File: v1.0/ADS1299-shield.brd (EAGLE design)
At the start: 63.5 x 25.4 mm, 32 parts, among them IC1 ADS1298*PAG*, IC2 TPS73250DBVT, IC3 TPS73233DBVT

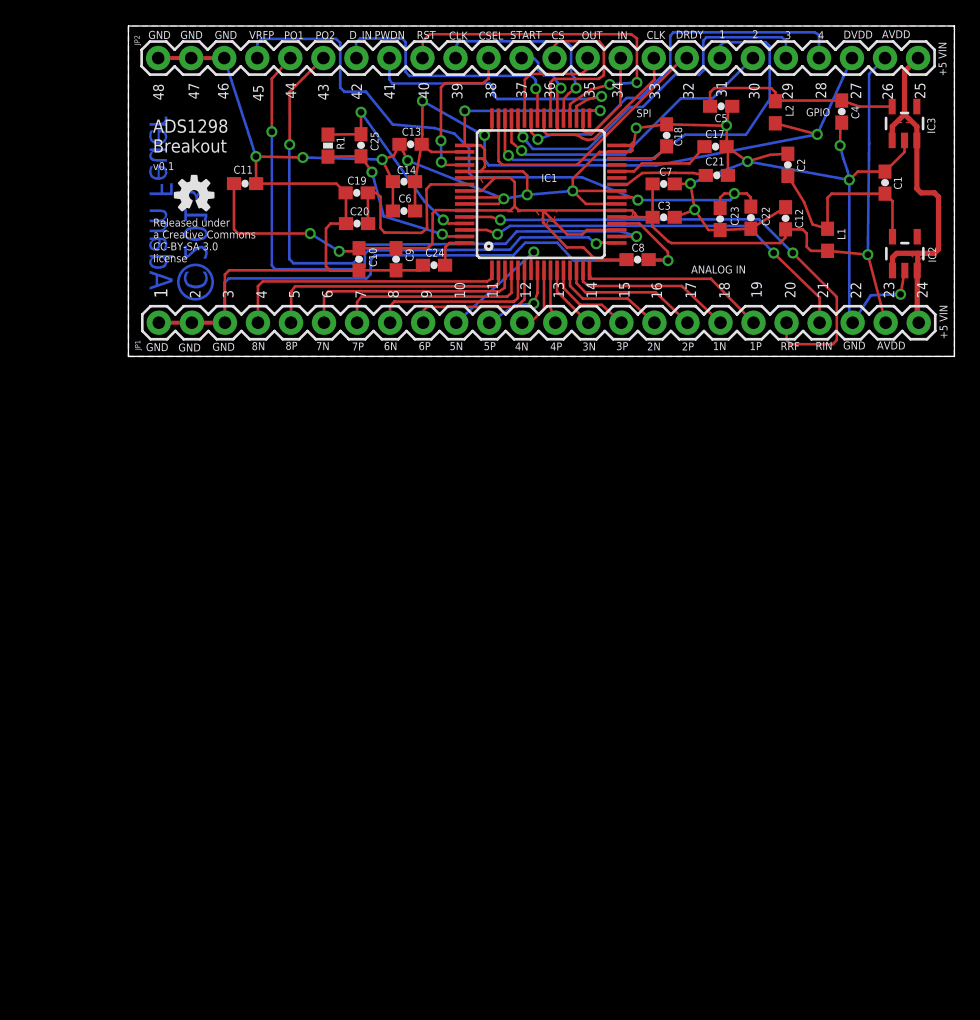
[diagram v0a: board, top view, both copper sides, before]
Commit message: schematic work - power supplies and decoupling done; updated ADS1299 library symbol to better organize pinouts; minor updates to power supply libraries
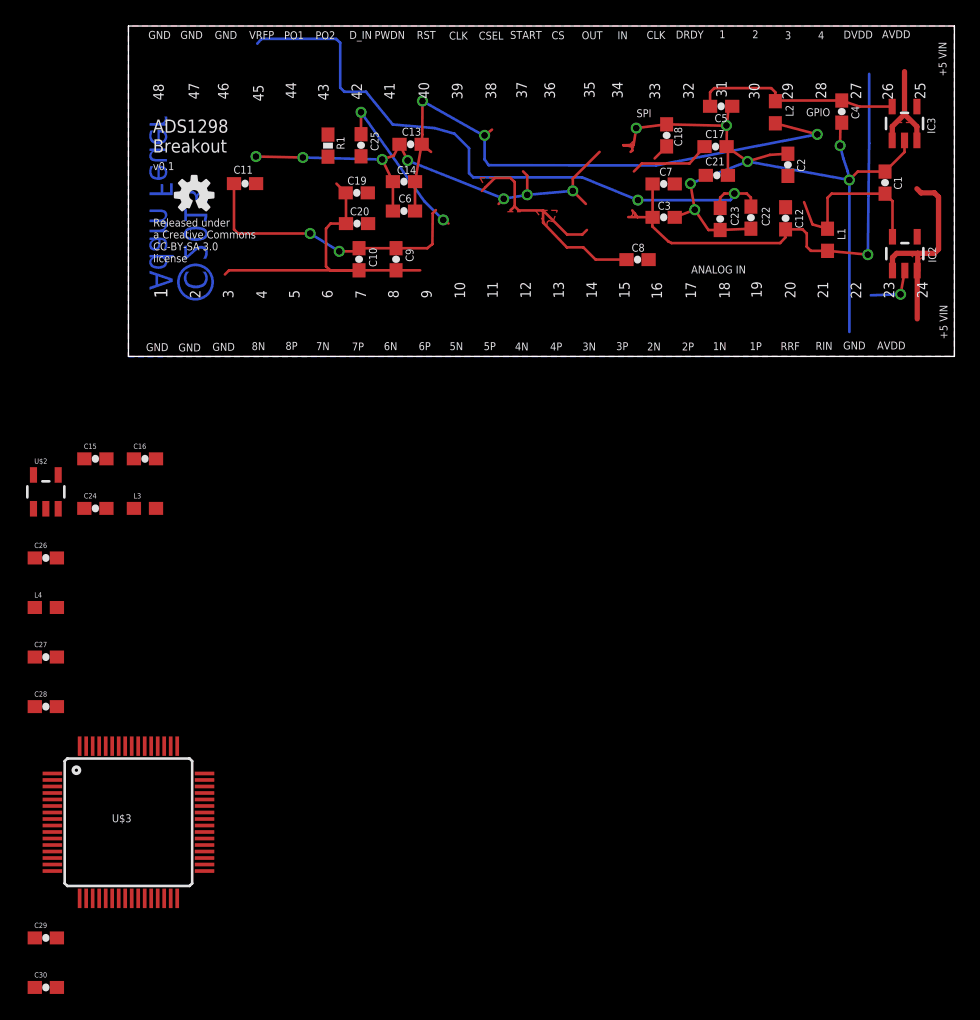
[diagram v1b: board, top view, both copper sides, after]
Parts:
- removed IC1: ADS1298*PAG*, burr-brown-5a:TQFP64
- removed JP1, JP2: M24, SparkFun-Connectors:1X24
- added C15: 2.2uF, SparkFun-Passives:0603-CAP
- added C16: 10 uF, SparkFun-Passives:0603-CAP
- added C26, C28, C29, C30: 1uF, SparkFun-Passives:0603-CAP
- added C27: 10uf, SparkFun-Passives:0603-CAP
- added L3, L4: 3.3 uH, SparkFun-Passives:0603
- added U$2: TPS604XXDBV, TPS604xx:SOT23-5
- added U$3: ADS1299*PAG*, ADS129x:TQFP64
- C17: value 22uF -> 100uF
- C24: value 100pF -> 10uf
- IC2: value TPS73250DBVT -> TPS73225DBVT
- moved C24 32.1 mm to (-2.54, -11.4), turned to 0 degrees
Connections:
- removed net PACEOUT1: IC1.17, JP2.6
- removed net PACEOUT2: IC1.18, JP2.7
- removed net RLD_IN: IC1.62, JP1.22
- removed net RLD_INV: C25.2, IC1.61, R1.2
- removed net RLD_OUT: C25.1, IC1.63, R1.1
- removed net RLD_REF: IC1.60, JP1.21
- removed net VCC: IC2.1, IC2.3, IC3.1, IC3.3, JP1.25, JP2.25
- new net AVSS: C11.2, C12.2, C29.2, C30.2, U$3.20, U$3.23, U$3.32, U$3.53, U$3.57, U$3.58
- new net BIASIN: U$3.62
- new net BIASINV: C25.2, R1.2, U$3.61
- new net BIASOUT: C25.1, R1.1, U$3.63
- new net BIASREF: U$3.60
- new net GND: C27.1, C28.1, C7.2, C8.2, IC2.1, IC2.3, IC3.1, IC3.3, L4.1
- new net N$10: C26.1, U$2.3
- new net N$12: L4.2, U$2.2
- new net N$9: C26.2, U$2.5
- new net SRB1: U$3.18
- new net SRB2: U$3.17
- new net VCC_-5V: C24.1, L3.2
- net !PWDN: now also U$3.35; no longer IC1.35, JP2.9
- net !RESET: now also U$3.36; no longer IC1.36, JP2.10
- net AGND: now also C15.2, C16.2, C27.2, C28.2, C29.1, C30.1, U$2.4, U$3.25, U$3.33, U$3.49, U$3.51; no longer C11.2, C12.2, C7.2, C8.2, IC1.20, IC1.23, IC1.25, IC1.31, IC1.32, IC1.33, IC1.49, IC1.51, IC1.53, IC1.57, IC1.58, JP1.2, JP1.23, JP1.3, JP1.4, JP2.2, JP2.3, JP2.4
- net AVDD: now also U$3.19, U$3.21, U$3.22, U$3.54, U$3.56, U$3.59; no longer IC1.19, IC1.21, IC1.22, IC1.54, IC1.56, IC1.59, JP1.24, JP2.24
- net CLK: now also U$3.37; no longer IC1.37, JP2.11
- net CLKSEL: now also U$3.52; no longer IC1.52, JP2.12
- net DAISY_IN: now also U$3.41; no longer IC1.41, JP2.8
- net DVDD: now also U$3.48, U$3.50; no longer IC1.48, IC1.50, JP2.23
- net GPIO1: now also U$3.42; no longer IC1.42, JP2.22
- net GPIO2: now also U$3.44; no longer IC1.44, JP2.21
- net GPIO3: now also U$3.45; no longer IC1.45, JP2.20
- net GPIO4: now also U$3.46; no longer IC1.46, JP2.19
- net IN1N: now also U$3.15; no longer IC1.15, JP1.19
- net IN1P: now also U$3.16; no longer IC1.16, JP1.20
- net IN2N: now also U$3.13; no longer IC1.13, JP1.17
- net IN2P: now also U$3.14; no longer IC1.14, JP1.18
- net IN3N: now also U$3.11; no longer IC1.11, JP1.15
- net IN3P: now also U$3.12; no longer IC1.12, JP1.16
- net IN4N: now also U$3.9; no longer IC1.9, JP1.13
- net IN4P: now also U$3.10; no longer IC1.10, JP1.14
- net IN5N: now also U$3.7; no longer IC1.7, JP1.11
- net IN5P: now also U$3.8; no longer IC1.8, JP1.12
- net IN6N: now also U$3.5; no longer IC1.5, JP1.9
- net IN6P: now also U$3.6; no longer IC1.6, JP1.10
- net IN7N: now also U$3.3; no longer IC1.3, JP1.7
- net IN7P: now also U$3.4; no longer IC1.4, JP1.8
- net IN8N: now also U$3.1; no longer IC1.1, JP1.5
- net IN8P: now also U$3.2; no longer IC1.2, JP1.6
- net N$3: now also U$3.28; no longer IC1.28
- net N$4: now also U$3.30; no longer IC1.30
- net N$5: now also U$3.55; no longer IC1.55
- net N$7: now also C15.1, C16.1, L3.1, U$2.1; no longer C24.1, IC1.64
- net N$8: now also U$3.26; no longer IC1.26
- net SPI_CLK: now also U$3.40; no longer IC1.40, JP2.17
- net SPI_CS: now also U$3.39; no longer IC1.39, JP2.14
- net SPI_DRDY: now also U$3.47; no longer IC1.47, JP2.18
- net SPI_IN: now also U$3.34; no longer IC1.34, JP2.16
- net SPI_OUT: now also U$3.43; no longer IC1.43, JP2.15
- net SPI_START: now also U$3.38; no longer IC1.38, JP2.13
- net VREFP: now also U$3.24; no longer IC1.24, JP2.5
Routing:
- net AGND: track 257.5 -> 133.2 mm, vias 18 -> 15
- net PACEOUT2: track 46.4 -> 0.00 mm, vias 2 -> 0
- net PACEOUT1: track 44.9 -> 0.00 mm, vias 2 -> 0
- net RLD_REF: track 39.9 -> 0.00 mm, vias 2 -> 0
- net GPIO4: track 34.4 -> 0.00 mm, vias 1 -> 0
- net RLD_IN: track 31.8 -> 0.00 mm, vias 2 -> 0
- net GPIO1: track 30.1 -> 0.00 mm, vias 1 -> 0
- net VCC: track 29.4 -> 0.00 mm
- net GPIO2: track 28.5 -> 0.00 mm, vias 1 -> 0
- net !RESET: track 28.1 -> 0.00 mm, vias 2 -> 0
- net AVDD: track 108.2 -> 81.7 mm
- net GND: track 0.00 -> 23.9 mm
- net GPIO3: track 23.8 -> 0.00 mm, vias 1 -> 0
- net !PWDN: track 22.0 -> 0.00 mm, vias 1 -> 0
- net IN8N: track 21.6 -> 0.00 mm
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
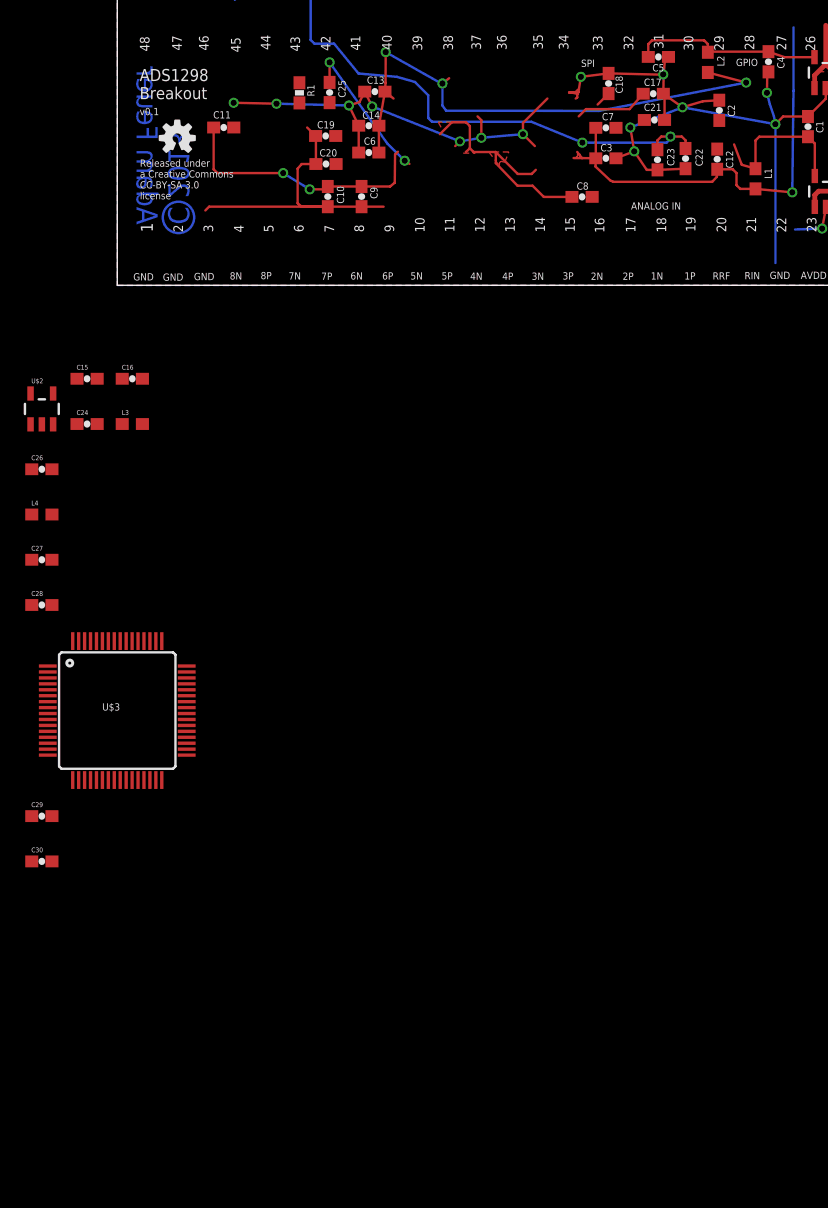
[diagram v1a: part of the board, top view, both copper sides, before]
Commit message: updated ads1299 library to have NAME and VALUE; improved power supply section, including supply-select jumpers
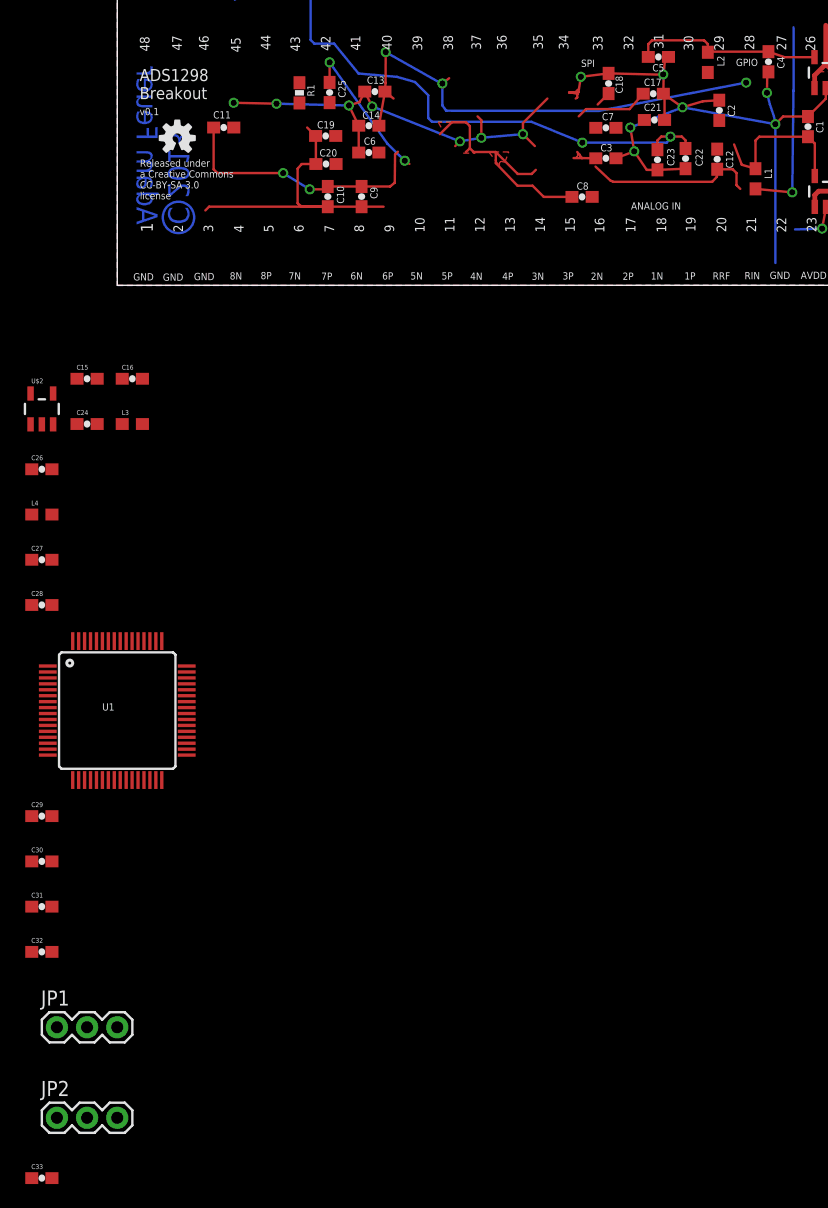
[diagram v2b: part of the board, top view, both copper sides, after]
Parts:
- added C31, C32: 1uF, SparkFun-Passives:0603-CAP
- added C33: 0.1uF, SparkFun-Passives:0603-CAP
- added JP1: AVDD_5V-2.5V, SparkFun-Passives:1X03
- added JP2: AVSS_-2.5V-GND, SparkFun-Passives:1X03
- IC2: value TPS73225DBVT -> TPS72325DBVT
- IC3: value TPS73233DBVT -> TPS73225DBVT
- U1: value ADS1299*PAG* -> ADS1299IPAG
- renumbered U$3 to U1
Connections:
- new net +2.5V: C6.1, JP1.3, L2.2
- new net -2.5V: C3.1, JP2.1, L1.2
- new net N$11: C32.1, IC3.4
- new net N$13: C31.1, IC2.4
- new net VCC_5V: C27.1, IC3.1, IC3.3, JP1.1, L4.1
- net AGND: now also C31.2, C32.2, JP2.3
- net AVDD: now also C33.1, JP1.2; no longer C3.1, L1.2
- net AVSS: now also C33.2, JP2.2
- net DVDD: no longer C6.1, L2.2
- net GND: no longer C27.1, C28.1, IC2.1, IC2.3, IC3.1, IC3.3, L4.1
- net VCC_-5V: now also C28.1, IC2.1, IC2.3
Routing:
- net AVDD: track 81.7 -> 57.6 mm, vias 3 -> 2
- net GND: track 23.9 -> 0.00 mm
- net -2.5V: track 0.00 -> 19.5 mm, vias 0 -> 1
- net VCC_-5V: track 0.00 -> 15.8 mm
- net VCC_5V: track 0.00 -> 8.09 mm
- net DVDD: track 46.9 -> 41.3 mm

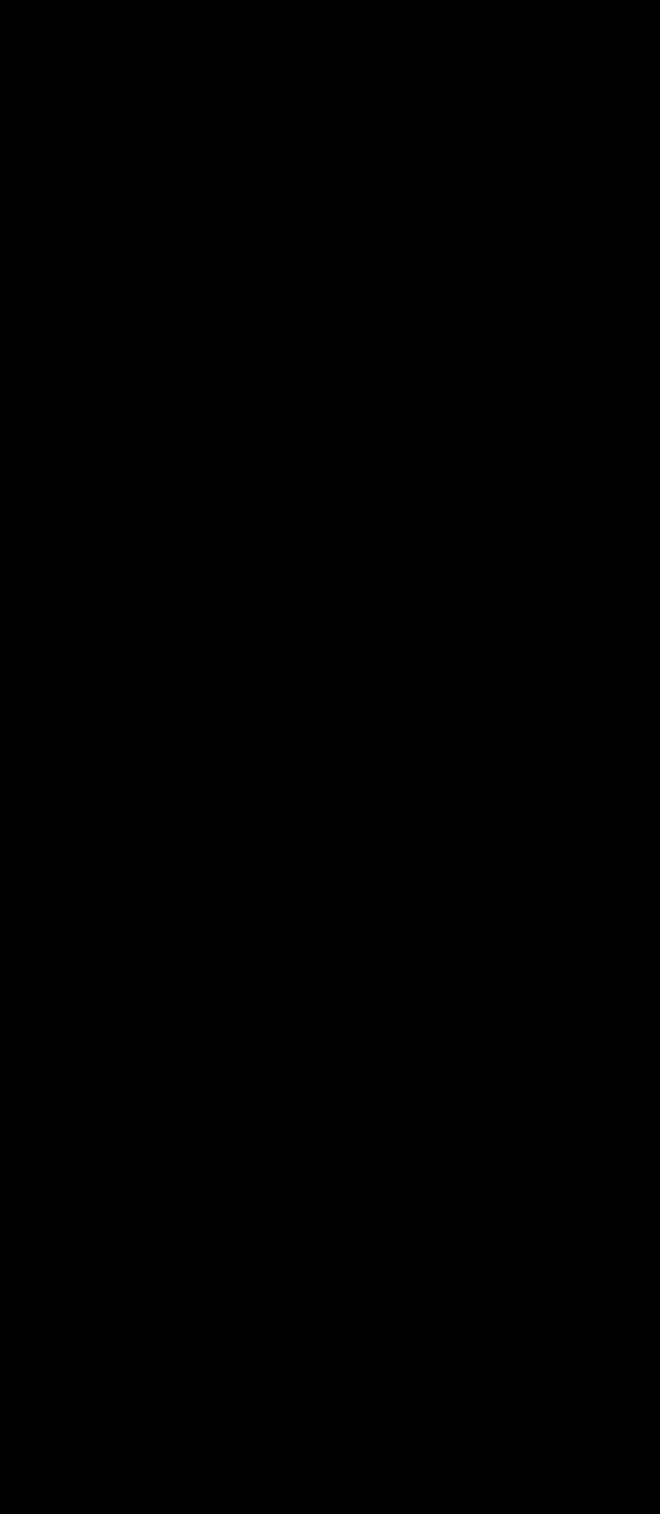
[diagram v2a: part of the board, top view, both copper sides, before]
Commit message: input filtering section done
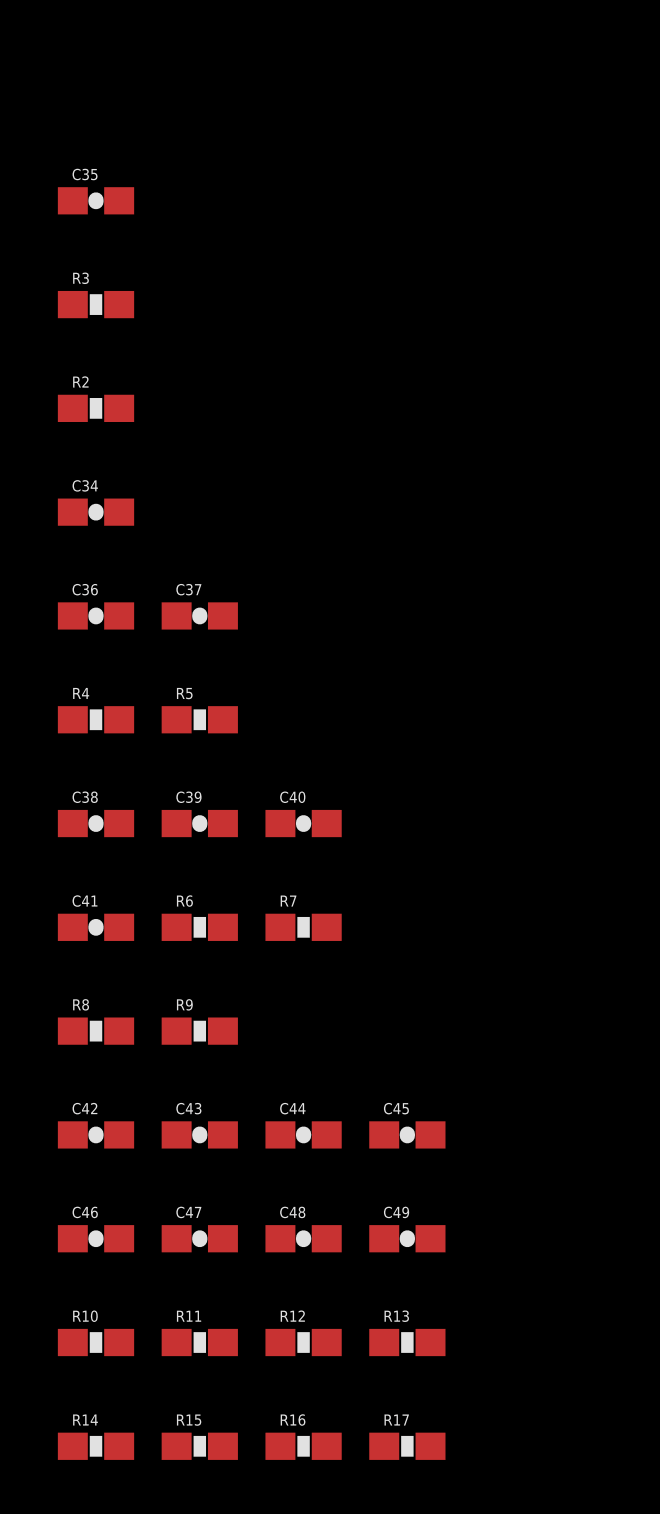
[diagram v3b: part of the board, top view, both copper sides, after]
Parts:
- added C34, C35, C36, C37, C38, C39, C40, C41, C42, C43, C44, C45, C46, C47, C48, C49: 4.7nF, SparkFun-Passives:0603-CAP
- added R10, R11, R12, R13, R14, R15, R16, R17, R2, R3, R4, R5, R6, R7, R8, R9: 4.99k, SparkFun-Passives:0603-RES
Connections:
- new net AIN1N: C34.2, C37.2, C43.2, R11.2, R2.2, R5.2
- new net AIN1P: C35.1, C36.1, R3.2, R4.2
- new net AIN3N: C39.2, R7.2
- new net AIN3P: C38.1, R6.2
- new net AIN4N: C41.2, R9.2
- new net AIN4P: C40.1, R8.2
- new net AIN5P: C42.1, R10.2
- new net AIN6N: C45.2, R13.2
- new net AIN6P: C44.1, R12.2
- new net AIN7N: C47.2, R15.2
- new net AIN7P: C46.1, R14.2
- new net AIN8N: C49.2, R17.2
- new net AIN8P: C48.1, R16.2
- net AGND: now also C34.1, C35.2, C36.2, C37.1, C38.2, C39.1, C40.2, C41.1, C42.2, C43.1, C44.2, C45.1, C46.2, C47.1, C48.2, C49.1
- net IN1N: now also R2.1, R5.1
- net IN1P: now also R3.1, R4.1
- net IN2N: now also R7.1
- net IN3P: now also R6.1
- net IN4N: now also R9.1
- net IN4P: now also R8.1
- net IN5N: now also R11.1
- net IN5P: now also R10.1
- net IN6N: now also R13.1
- net IN6P: now also R12.1
- net IN7N: now also R15.1
- net IN7P: now also R14.1
- net IN8N: now also R17.1
- net IN8P: now also R16.1
